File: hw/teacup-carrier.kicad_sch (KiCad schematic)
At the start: 133 parts, among them J1 AH58893-T9B10-3F, J2 TYPE-C-31-M-12, J20 HDR_J20, J21 HDR_J21, J22 HDR_J22, J23 HDR_J23, J24 HDR_J24, J25 HDR_J25, J26 HDR_J26, J27 HDR_J27, J28 HDR_J28, J29 HDR_J29, J3 TE_292303-7, J30 HDR_J30, J31 HDR_J31, J32 HDR_J32, J33 HDR_J33, J34 HDR_J34, J35 HDR_J35, J36 HDR_J36, J37 HDR_J37, J38 AMP_MIC_TAP, J4 Hirose_DM3D-SF, J5 Wuerth_694106301002, J6 AudioJack4_Ground, J7 SFW15R-2STE1LF, J8 SFW15R-2STE1LF, J9 TYPE-C-31-M-12, Q1 AO3401A, Q2 AO3401A, SW1 SSSS711403, SW2 SSSS711403, U1 AP62600SJ-7, U10 TS5A3166, U11 DIP-8 Socket, U12 TPS2053BDR, U13 W25Q32JVSS, U14 TPS22990DMLR, U15 TCA9555PWR, U2 AP62300WU-7, U3 MCP4661-104E_ST, U4 TPS22990DMLR, U5 AZ1117CH-3.3TRG1, U6 AZ1117CH-1.8TRG1, U7 AP62300WU-7, U8 ESP32-S3-WROOM-1-N16R2, U9 TS5A3166

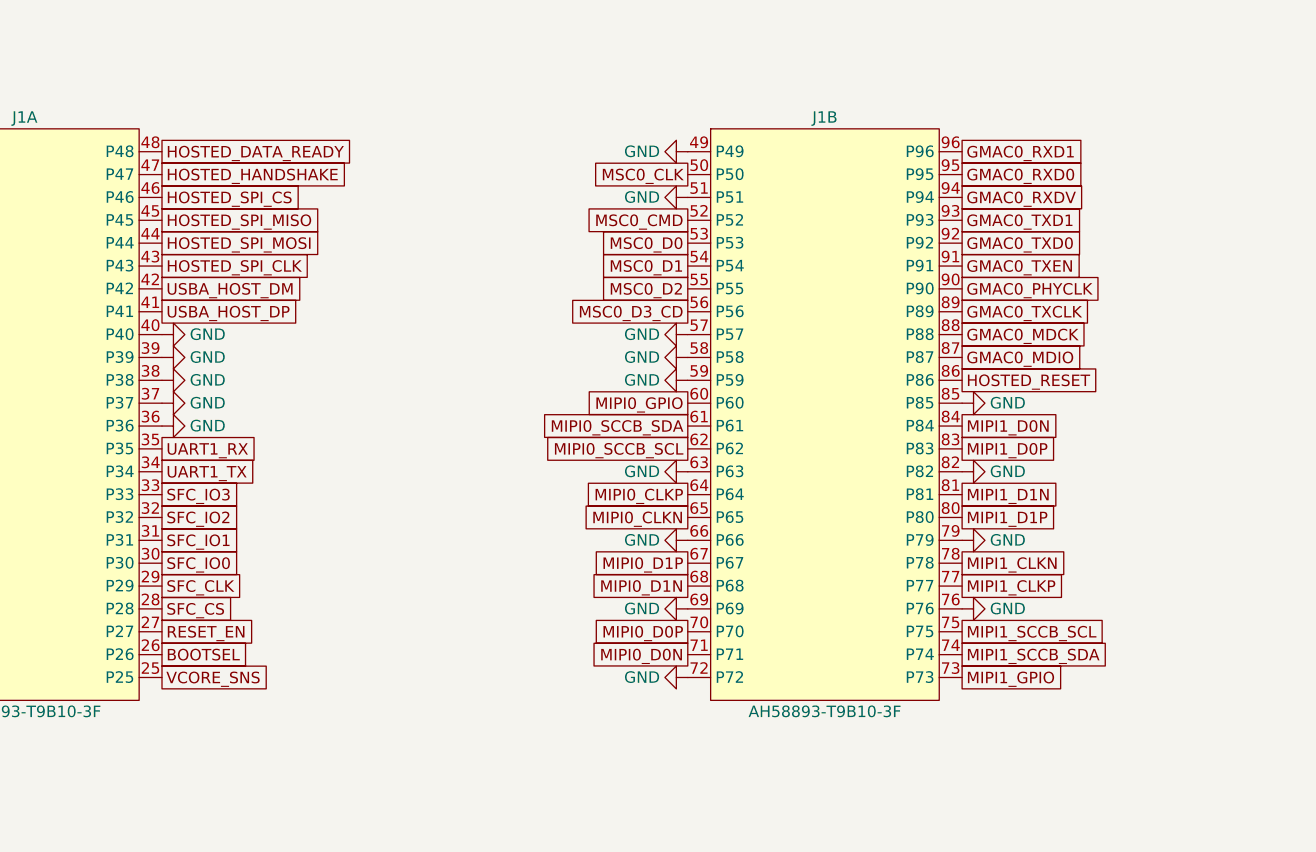
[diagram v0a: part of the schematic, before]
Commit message: Reorder J1 MSC0/USB-host/ESP-hosted/MIPI1 pins for board-order and grouping
- MSC0 (J1 pins 50/52-56): reordered to match J4's microSD pins in
  actual left-to-right board position (D1/D0/CLK/CMD/D3_CD/D2), not
  J4's raw pin numbers -- J4 sits mirrored relative to J1 on the real
  board, so matching by pin number alone produced a fully-crossed
  assignment.
- USBA_HOST_DP/DM shifted down to pins 40/41, freeing pin 42 for
  HOSTED_RESET so all ESP-Hosted signals (reset + SPI + handshake) are
  one contiguous block (42-48) instead of HOSTED_RESET sitting alone at
  unit 2 pin 86. Pin 86 is now GND.
- MIPI1 pins 73-75 rotated (GPIO/SDA/SCL -> SDA/SCL/GPIO) to match
  MIPI0's arrangement.

PCB updated to match: pad nets reassigned for all of the above, and the
already-routed MSC0/MIPI1 SDA+SCL traces had their J1-side endpoints
moved to the new pad positions rather than left stale. GND zone
refilled and DRC-clean for all touched nets.
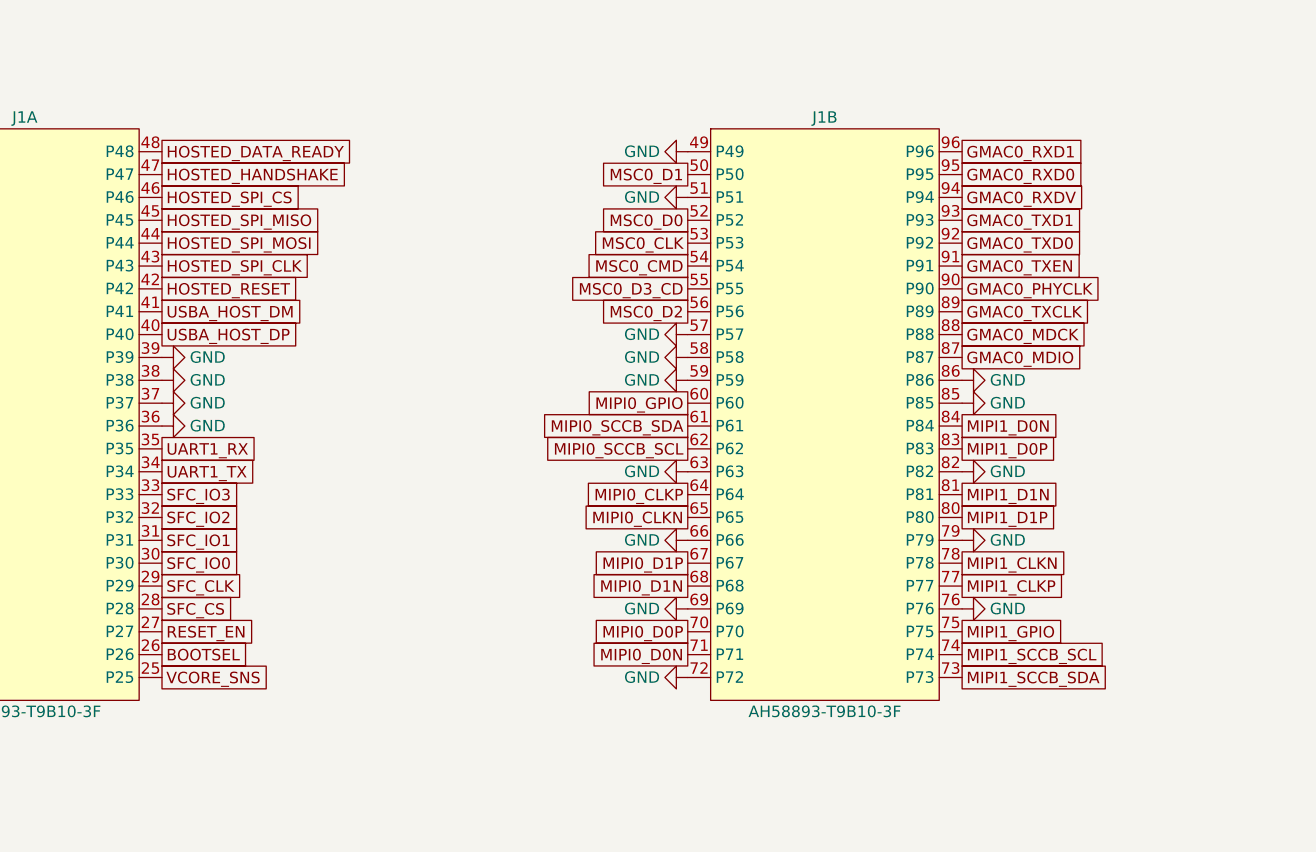
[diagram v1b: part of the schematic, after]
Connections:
- net GND: now also J1.86 (P86); no longer J1.40 (P40)
- net HOSTED_RESET: now also J1.42 (P42); no longer J1.86 (P86)
- net MIPI1_GPIO: now also J1.75 (P75); no longer J1.73 (P73)
- net MIPI1_SCCB_SCL: now also J1.74 (P74); no longer J1.75 (P75)
- net MIPI1_SCCB_SDA: now also J1.73 (P73); no longer J1.74 (P74)
- net MSC0_CLK: now also J1.53 (P53); no longer J1.50 (P50)
- net MSC0_CMD: now also J1.54 (P54); no longer J1.52 (P52)
- net MSC0_D0: now also J1.52 (P52); no longer J1.53 (P53)
- net MSC0_D1: now also J1.50 (P50); no longer J1.54 (P54)
- net MSC0_D2: now also J1.56 (P56); no longer J1.55 (P55)
- net MSC0_D3_CD: now also J1.55 (P55); no longer J1.56 (P56)
- net USBA_HOST_DM: now also J1.41 (P41); no longer J1.42 (P42)
- net USBA_HOST_DP: now also J1.40 (P40); no longer J1.41 (P41)
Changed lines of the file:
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@@
 		(property "Value" "GND" (at 71.12 378.46 270) (effects (font (size 1.27 1.27))))
-	)
-	(symbol (lib_id "power:GND") (at 66.04 375.92 90) (unit 1)
-		(property "Reference" "#CGND015" (at 66.04 375.92 0) (effects (font (size 1.27 1.27)) hide))
-		(property "Value" "GND" (at 71.12 375.92 270) (effects (font (size 1.27 1.27))))
 	)
 	(symbol (lib_id "teacup-carrier:AH58893-T9B10-3F") (at 139.7 384.81 0) (unit 2)
@@
 	)
 	(symbol (lib_id "power:GND") (at 124.46 355.6 270) (unit 1)
-		(property "Reference" "#CGND016" (at 124.46 355.6 0) (effects (font (size 1.27 1.27)) hide))
+		(property "Reference" "#CGND015" (at 124.46 355.6 0) (effects (font (size 1.27 1.27)) hide))
 		(property "Value" "GND" (at 119.38 355.6 90) (effects (font (size 1.27 1.27))))
 	)
 	(symbol (lib_id "power:GND") (at 124.46 360.68 270) (unit 1)
-		(property "Reference" "#CGND017" (at 124.46 360.68 0) (effects (font (size 1.27 1.27)) hide))
+		(property "Reference" "#CGND016" (at 124.46 360.68 0) (effects (font (size 1.27 1.27)) hide))
 		(property "Value" "GND" (at 119.38 360.68 90) (effects (font (size 1.27 1.27))))
 	)
 	(symbol (lib_id "power:GND") (at 124.46 375.92 270) (unit 1)
-		(property "Reference" "#CGND018" (at 124.46 375.92 0) (effects (font (size 1.27 1.27)) hide))
+		(property "Reference" "#CGND017" (at 124.46 375.92 0) (effects (font (size 1.27 1.27)) hide))
 		(property "Value" "GND" (at 119.38 375.92 90) (effects (font (size 1.27 1.27))))
 	)
 	(symbol (lib_id "power:GND") (at 124.46 378.46 270) (unit 1)
-		(property "Reference" "#CGND019" (at 124.46 378.46 0) (effects (font (size 1.27 1.27)) hide))
+		(property "Reference" "#CGND018" (at 124.46 378.46 0) (effects (font (size 1.27 1.27)) hide))
 		(property "Value" "GND" (at 119.38 378.46 90) (effects (font (size 1.27 1.27))))
 	)
 	(symbol (lib_id "power:GND") (at 124.46 381 270) (unit 1)
-		(property "Reference" "#CGND020" (at 124.46 381 0) (effects (font (size 1.27 1.27)) hide))
+		(property "Reference" "#CGND019" (at 124.46 381 0) (effects (font (size 1.27 1.27)) hide))
 		(property "Value" "GND" (at 119.38 381 90) (effects (font (size 1.27 1.27))))
 	)
 	(symbol (lib_id "power:GND") (at 124.46 391.16 270) (unit 1)
-		(property "Reference" "#CGND021" (at 124.46 391.16 0) (effects (font (size 1.27 1.27)) hide))
+		(property "Reference" "#CGND020" (at 124.46 391.16 0) (effects (font (size 1.27 1.27)) hide))
 		(property "Value" "GND" (at 119.38 391.16 90) (effects (font (size 1.27 1.27))))
 	)
 	(symbol (lib_id "power:GND") (at 124.46 398.78 270) (unit 1)
-		(property "Reference" "#CGND022" (at 124.46 398.78 0) (effects (font (size 1.27 1.27)) hide))
+		(property "Reference" "#CGND021" (at 124.46 398.78 0) (effects (font (size 1.27 1.27)) hide))
 		(property "Value" "GND" (at 119.38 398.78 90) (effects (font (size 1.27 1.27))))
 	)
 	(symbol (lib_id "power:GND") (at 124.46 406.4 270) (unit 1)
-		(property "Reference" "#CGND023" (at 124.46 406.4 0) (effects (font (size 1.27 1.27)) hide))
+		(property "Reference" "#CGND022" (at 124.46 406.4 0) (effects (font (size 1.27 1.27)) hide))
 		(property "Value" "GND" (at 119.38 406.4 90) (effects (font (size 1.27 1.27))))
 	)
 	(symbol (lib_id "power:GND") (at 124.46 414.02 270) (unit 1)
-		(property "Reference" "#CGND024" (at 124.46 414.02 0) (effects (font (size 1.27 1.27)) hide))
+		(property "Reference" "#CGND023" (at 124.46 414.02 0) (effects (font (size 1.27 1.27)) hide))
 		(property "Value" "GND" (at 119.38 414.02 90) (effects (font (size 1.27 1.27))))
 	)
 	(symbol (lib_id "power:GND") (at 154.94 406.4 90) (unit 1)
-		(property "Reference" "#CGND025" (at 154.94 406.4 0) (effects (font (size 1.27 1.27)) hide))
+		(property "Reference" "#CGND024" (at 154.94 406.4 0) (effects (font (size 1.27 1.27)) hide))
 		(property "Value" "GND" (at 160.02 406.4 270) (effects (font (size 1.27 1.27))))
 	)
 	(symbol (lib_id "power:GND") (at 154.94 398.78 90) (unit 1)
-		(property "Reference" "#CGND026" (at 154.94 398.78 0) (effects (font (size 1.27 1.27)) hide))
+		(property "Reference" "#CGND025" (at 154.94 398.78 0) (effects (font (size 1.27 1.27)) hide))
 		(property "Value" "GND" (at 160.02 398.78 270) (effects (font (size 1.27 1.27))))
 	)
 	(symbol (lib_id "power:GND") (at 154.94 391.16 90) (unit 1)
-		(property "Reference" "#CGND027" (at 154.94 391.16 0) (effects (font (size 1.27 1.27)) hide))
+		(property "Reference" "#CGND026" (at 154.94 391.16 0) (effects (font (size 1.27 1.27)) hide))
 		(property "Value" "GND" (at 160.02 391.16 270) (effects (font (size 1.27 1.27))))
 	)
 	(symbol (lib_id "power:GND") (at 154.94 383.54 90) (unit 1)
-		(property "Reference" "#CGND028" (at 154.94 383.54 0) (effects (font (size 1.27 1.27)) hide))
+		(property "Reference" "#CGND027" (at 154.94 383.54 0) (effects (font (size 1.27 1.27)) hide))
 		(property "Value" "GND" (at 160.02 383.54 270) (effects (font (size 1.27 1.27))))
+	)
+	(symbol (lib_id "power:GND") (at 154.94 381 90) (unit 1)
+		(property "Reference" "#CGND028" (at 154.94 381 0) (effects (font (size 1.27 1.27)) hide))
+		(property "Value" "GND" (at 160.02 381 270) (effects (font (size 1.27 1.27))))
 	)
 	(symbol (lib_id "teacup-carrier:AH58893-T9B10-3F") (at 228.6 384.81 0) (unit 3)
@@
 	(global_label "UART1_TX" (at 66.04 391.16 0) (effects (font (size 1.27 1.27)) (justify left)))
 	(global_label "UART1_RX" (at 66.04 388.62 0) (effects (font (size 1.27 1.27)) (justify left)))
-	(global_label "USBA_HOST_DP" (at 66.04 373.38 0) (effects (font (size 1.27 1.27)) (justify left)))
-	(global_label "USBA_HOST_DM" (at 66.04 370.84 0) (effects (font (size 1.27 1.27)) (justify left)))
+	(global_label "USBA_HOST_DP" (at 66.04 375.92 0) (effects (font (size 1.27 1.27)) (justify left)))
+	(global_label "USBA_HOST_DM" (at 66.04 373.38 0) (effects (font (size 1.27 1.27)) (justify left)))
+	(global_label "HOSTED_RESET" (at 66.04 370.84 0) (effects (font (size 1.27 1.27)) (justify left)))
 	(global_label "HOSTED_SPI_CLK" (at 66.04 368.3 0) (effects (font (size 1.27 1.27)) (justify left)))
 	(global_label "HOSTED_SPI_MOSI" (at 66.04 365.76 0) (effects (font (size 1.27 1.27)) (justify left)))
@@
 	(global_label "HOSTED_HANDSHAKE" (at 66.04 358.14 0) (effects (font (size 1.27 1.27)) (justify left)))
 	(global_label "HOSTED_DATA_READY" (at 66.04 355.6 0) (effects (font (size 1.27 1.27)) (justify left)))
-	(global_label "MSC0_CLK" (at 124.46 358.14 180) (effects (font (size 1.27 1.27)) (justify right)))
-	(global_label "MSC0_CMD" (at 124.46 363.22 180) (effects (font (size 1.27 1.27)) (justify right)))
-	(global_label "MSC0_D0" (at 124.46 365.76 180) (effects (font (size 1.27 1.27)) (justify right)))
-	(global_label "MSC0_D1" (at 124.46 368.3 180) (effects (font (size 1.27 1.27)) (justify right)))
-	(global_label "MSC0_D2" (at 124.46 370.84 180) (effects (font (size 1.27 1.27)) (justify right)))
-	(global_label "MSC0_D3_CD" (at 124.46 373.38 180) (effects (font (size 1.27 1.27)) (justify right)))
+	(global_label "MSC0_D1" (at 124.46 358.14 180) (effects (font (size 1.27 1.27)) (justify right)))
+	(global_label "MSC0_D0" (at 124.46 363.22 180) (effects (font (size 1.27 1.27)) (justify right)))
+	(global_label "MSC0_CLK" (at 124.46 365.76 180) (effects (font (size 1.27 1.27)) (justify right)))
+	(global_label "MSC0_CMD" (at 124.46 368.3 180) (effects (font (size 1.27 1.27)) (justify right)))
+	(global_label "MSC0_D3_CD" (at 124.46 370.84 180) (effects (font (size 1.27 1.27)) (justify right)))
+	(global_label "MSC0_D2" (at 124.46 373.38 180) (effects (font (size 1.27 1.27)) (justify right)))
 	(global_label "MIPI0_GPIO" (at 124.46 383.54 180) (effects (font (size 1.27 1.27)) (justify right)))
 	(global_label "MIPI0_SCCB_SDA" (at 124.46 386.08 180) (effects (font (size 1.27 1.27)) (justify right)))
@@
 	(global_label "MIPI0_D0P" (at 124.46 408.94 180) (effects (font (size 1.27 1.27)) (justify right)))
 	(global_label "MIPI0_D0N" (at 124.46 411.48 180) (effects (font (size 1.27 1.27)) (justify right)))
-	(global_label "MIPI1_GPIO" (at 154.94 414.02 0) (effects (font (size 1.27 1.27)) (justify left)))
-	(global_label "MIPI1_SCCB_SDA" (at 154.94 411.48 0) (effects (font (size 1.27 1.27)) (justify left)))
-	(global_label "MIPI1_SCCB_SCL" (at 154.94 408.94 0) (effects (font (size 1.27 1.27)) (justify left)))
+	(global_label "MIPI1_SCCB_SDA" (at 154.94 414.02 0) (effects (font (size 1.27 1.27)) (justify left)))
+	(global_label "MIPI1_SCCB_SCL" (at 154.94 411.48 0) (effects (font (size 1.27 1.27)) (justify left)))
+	(global_label "MIPI1_GPIO" (at 154.94 408.94 0) (effects (font (size 1.27 1.27)) (justify left)))
 	(global_label "MIPI1_CLKP" (at 154.94 403.86 0) (effects (font (size 1.27 1.27)) (justify left)))
 	(global_label "MIPI1_CLKN" (at 154.94 401.32 0) (effects (font (size 1.27 1.27)) (justify left)))
@@
 	(global_label "MIPI1_D0P" (at 154.94 388.62 0) (effects (font (size 1.27 1.27)) (justify left)))
 	(global_label "MIPI1_D0N" (at 154.94 386.08 0) (effects (font (size 1.27 1.27)) (justify left)))
-	(global_label "HOSTED_RESET" (at 154.94 381 0) (effects (font (size 1.27 1.27)) (justify left)))
 	(global_label "GMAC0_MDIO" (at 154.94 378.46 0) (effects (font (size 1.27 1.27)) (justify left)))
 	(global_label "GMAC0_MDCK" (at 154.94 375.92 0) (effects (font (size 1.27 1.27)) (justify left)))
